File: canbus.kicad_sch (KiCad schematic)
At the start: 18 parts, among them J501 Conn_01x02, J601 Conn_01x04, U203 ISO1050DUB, U204 TPD2E007, U603 H7550-H#

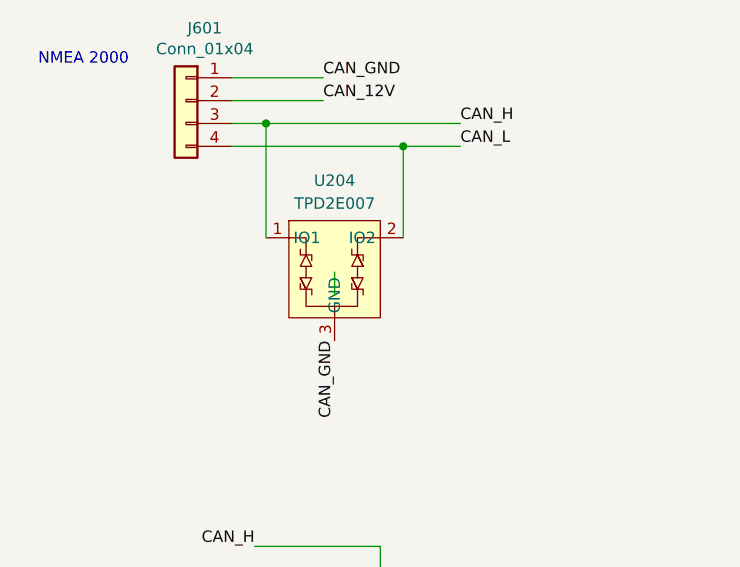
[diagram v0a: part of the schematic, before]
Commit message: Change buck converter to LMR54410
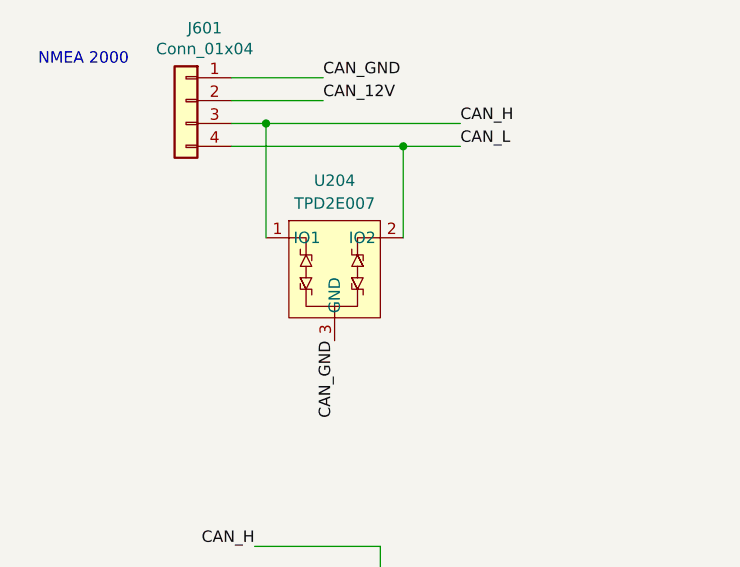
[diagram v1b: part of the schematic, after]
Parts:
- U603: footprint Package_TO_SOT_SMD:SOT-23 -> Package_TO_SOT_SMD:SOT-23-3
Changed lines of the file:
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@@
 	(title_block
 		(title "SH-ESP32")
-		(date "2024-06-27")
-		(rev "2.1.0")
+		(date "2024-09-24")
+		(rev "2.2.0")
 		(company "Hat Labs Oy")
 		(comment 1 "https://creativecommons.org/licenses/by-sa/4.0")
@@
 		(pts
 			(xy 50.8 58.42) (xy 72.39 58.42)
-		)
-		(stroke
-			(width 0)
-			(type default)
-		)
-	)
-	(wire
-		(pts
-			(xy 58.42 74.93) (xy 58.42 77.47)
 		)
 		(stroke
@@
 			)
 		)
-		(property "Description" ""
+		(property "Description" "Power symbol creates a global label with name \"GND\" , ground"
 			(at 165.1 111.76 0)
 			(effects
@@
 			)
 		)
-		(property "Description" ""
+		(property "Description" "Power symbol creates a global label with name \"GND\" , ground"
 			(at 156.21 95.25 0)
 			(effects
@@
 			)
 		)
-		(property "Description" ""
+		(property "Description" "Power symbol creates a global label with name \"+3.3V\""
 			(at 162.56 86.36 0)
 			(effects
@@
 			)
 		)
-		(property "Footprint" "Package_TO_SOT_SMD:SOT-23"
+		(property "Footprint" "Package_TO_SOT_SMD:SOT-23-3"
 			(at 177.8 31.115 0)
 			(effects
@@
 			)
 		)
-		(property "Datasheet" ""
+		(property "Datasheet" "https://www.holtek.com/documents/10179/116711/HT75xx-1v250.pdf"
 			(at 177.8 36.83 0)
 			(effects
@@
 			)
 		)
-		(property "Description" ""
+		(property "Description" "100mA Low Dropout Voltage Regulator, Fixed Output, SOT89"
 			(at 177.8 39.37 0)
 			(effects
@@
 			)
 		)
-		(property "Description" ""
+		(property "Description" "Special symbol for telling ERC where power comes from"
 			(at 156.21 36.83 0)
 			(effects
@@
 			)
 		)
-		(property "Description" ""
+		(property "Description" "Special symbol for telling ERC where power comes from"
 			(at 177.8 48.26 0)
 			(effects
@@
 			)
 		)
-		(property "Description" ""
+		(property "Description" "Power symbol creates a global label with name \"+3.3V\""
 			(at 139.7 88.9 0)
 			(effects

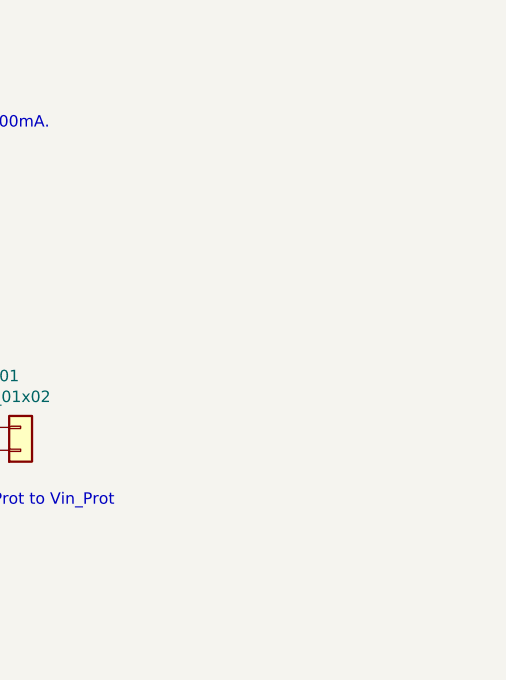
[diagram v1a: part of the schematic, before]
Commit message: Add a CAN power indicator LED
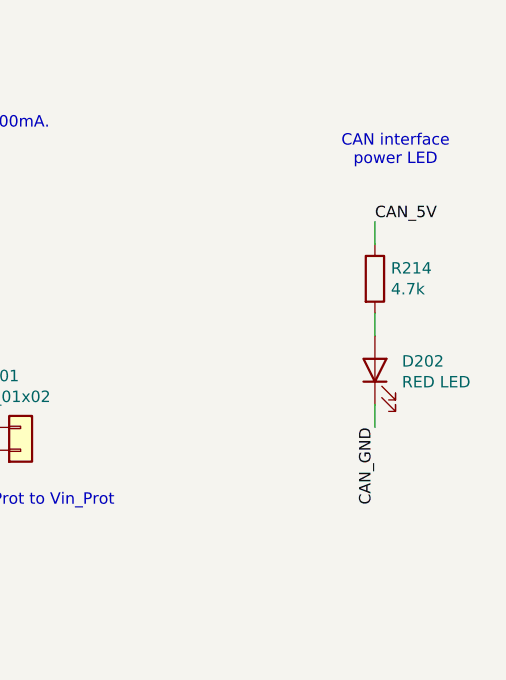
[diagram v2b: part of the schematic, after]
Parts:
- added D202: RED LED, LED_SMD:LED_0603_1608Metric, symbol Device:LED
- added R214: 4.7k, Resistor_SMD:R_0402_1005Metric, symbol Device:R
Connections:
- net CAN_5V: now also R214.1
- net CAN_GND: now also D202.1 (K)
- new net: D202.2 (A), R214.2
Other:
- note added: "CAN interface power LED"
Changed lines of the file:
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@@
+	(wire
+		(pts
+			(xy 259.08 50.8) (xy 259.08 53.34)
+		)
+		(stroke
+			(width 0)
+			(type default)
+		)
+	)
 	(wire
 		(pts
@@
 	(wire
 		(pts
+			(xy 259.08 63.5) (xy 259.08 60.96)
+		)
+		(stroke
+			(width 0)
+			(type default)
+		)
+	)
+	(wire
+		(pts
 			(xy 50.8 114.3) (xy 53.34 114.3)
 		)
@@
 	(wire
 		(pts
+			(xy 259.08 40.64) (xy 259.08 43.18)
+		)
+		(stroke
+			(width 0)
+			(type default)
+		)
+	)
+	(wire
+		(pts
 			(xy 194.31 41.91) (xy 194.31 36.83)
 		)
@@
 			)
 			(justify left bottom)
+		)
+	)
+	(text "CAN interface\npower LED"
+		(exclude_from_sim no)
+		(at 261.366 32.766 0)
+		(effects
+			(font
+				(size 1.27 1.27)
+			)
 		)
 	)
@@
 	)
 	(label "CAN_GND"
+		(at 259.08 63.5 270)
+		(fields_autoplaced yes)
+		(effects
+			(font
+				(size 1.27 1.27)
+			)
+			(justify right bottom)
+		)
+	)
+	(label "CAN_GND"
 		(at 194.31 101.6 0)
 		(fields_autoplaced yes)
@@
 	(label "CAN_GND"
 		(at 57.15 53.34 0)
+		(fields_autoplaced yes)
+		(effects
+			(font
+				(size 1.27 1.27)
+			)
+			(justify left bottom)
+		)
+	)
+	(label "CAN_5V"
+		(at 259.08 40.64 0)
 		(fields_autoplaced yes)
 		(effects
@@
 	)
 	(symbol
+		(lib_id "Device:LED")
+		(at 259.08 57.15 90)
+		(unit 1)
+		(exclude_from_sim no)
+		(in_bom yes)
+		(on_board yes)
+		(dnp no)
+		(property "Reference" "D202"
+			(at 262.0772 56.1594 90)
+			(effects
+				(font
+					(size 1.27 1.27)
+				)
+				(justify right)
+			)
+		)
+		(property "Value" "RED LED"
+			(at 262.0772 58.4708 90)
+			(effects
+				(font
+					(size 1.27 1.27)
+				)
+				(justify right)
+			)
+		)
+		(property "Footprint" "LED_SMD:LED_0603_1608Metric"
+			(at 259.08 57.15 0)
+			(effects
+				(font
+					(size 1.27 1.27)
+				)
+				(hide yes)
+			)
+		)
+		(property "Datasheet" "~"
+			(at 259.08 57.15 0)
+			(effects
+				(font
+					(size 1.27 1.27)
+				)
+				(hide yes)
+			)
+		)
+		(property "Description" ""
+			(at 259.08 57.15 0)
+			(effects
+				(font
+					(size 1.27 1.27)
+				)
+				(hide yes)
+			)
+		)
+		(property "LCSC" "C2286"
+			(at 259.08 57.15 0)
+			(effects
+				(font
+					(size 1.27 1.27)
+				)
+				(hide yes)
+			)
+		)
+		(property "JLCPCB_CORRECTION" ""
+			(at 259.08 57.15 0)
+			(effects
+				(font
+					(size 1.27 1.27)
+				)
+				(hide yes)
+			)
+		)
+		(pin "1"
+		)
+		(pin "2"
+		)
+		(instances
+			(project "SH-ESP32"
+				(path "/dff502f1-2fe5-4c09-a767-aabc78c2e052/00000000-0000-0000-0000-00005f733ba4"
+					(reference "D202")
+					(unit 1)
+				)
+			)
+		)
+	)
+	(symbol
 		(lib_id "power:+3.3V")
 		(at 139.7 88.9 0)
@@
 					(unit 1)
 				)
+			)
+		)
+	)
+	(symbol
+		(lib_id "Device:R")
+		(at 259.08 46.99 0)
+		(unit 1)
+		(exclude_from_sim no)
+		(in_bom yes)
+		(on_board yes)
+		(dnp no)
+		(property "Reference" "R214"
+			(at 260.858 45.8216 0)
+			(effects
+				(font
+					(size 1.27 1.27)
+				)
+				(justify left)
+			)
+		)
+		(property "Value" "4.7k"
+			(at 260.858 48.133 0)
+			(effects
+				(font
+					(size 1.27 1.27)
+				)
+				(justify left)
+			)
+		)
+		(property "Footprint" "Resistor_SMD:R_0402_1005Metric"
+			(at 257.302 46.99 90)
+			(effects
+				(font
+					(size 1.27 1.27)
+				)
+				(hide yes)
+			)
+		)
+		(property "Datasheet" "~"
+			(at 259.08 46.99 0)
+			(effects
+				(font
+					(size 1.27 1.27)
+				)
+				(hide yes)
+			)
+		)
+		(property "Description" ""
+			(at 259.08 46.99 0)
+			(effects
+				(font
+					(size 1.27 1.27)
+				)
+				(hide yes)
+			)
+		)
+		(property "LCSC" "C25900"
+			(at 259.08 46.99 0)
+			(effects
+				(font
+					(size 1.27 1.27)
+				)
+				(hide yes)
+			)
+		)
+		(property "JLCPCB_CORRECTION" ""
+			(at 259.08 46.99 0)
+			(effects
+				(font
+					(size 1.27 1.27)
+				)
+				(hide yes)
+			)
+		)
+		(pin "1"
+		)
+		(pin "2"
+		)
+		(instances
+			(project "SH-ESP32"
+				(path "/dff502f1-2fe5-4c09-a767-aabc78c2e052/00000000-0000-0000-0000-00005f733ba4"
+					(reference "R214")
+					(unit 1)
+				)
